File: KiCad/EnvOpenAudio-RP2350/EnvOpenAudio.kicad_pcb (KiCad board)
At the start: 2 copper layers, 21.3 x 68.7 mm, 69 parts, among them J1 USB_C_Receptacle_USB2.0, J2 SM03B-SRSS-TB, J3 Conn_01x10, SW1 B3U-1000, SW2 B3U-1000, U1 W25Q16JVUXIQ, U2 TPS63001DRCR, U3 TLV75518PDBV, U4 RP2350_60QFN, U5 TLV320AIC3100, Y1 ABM8-272-T3

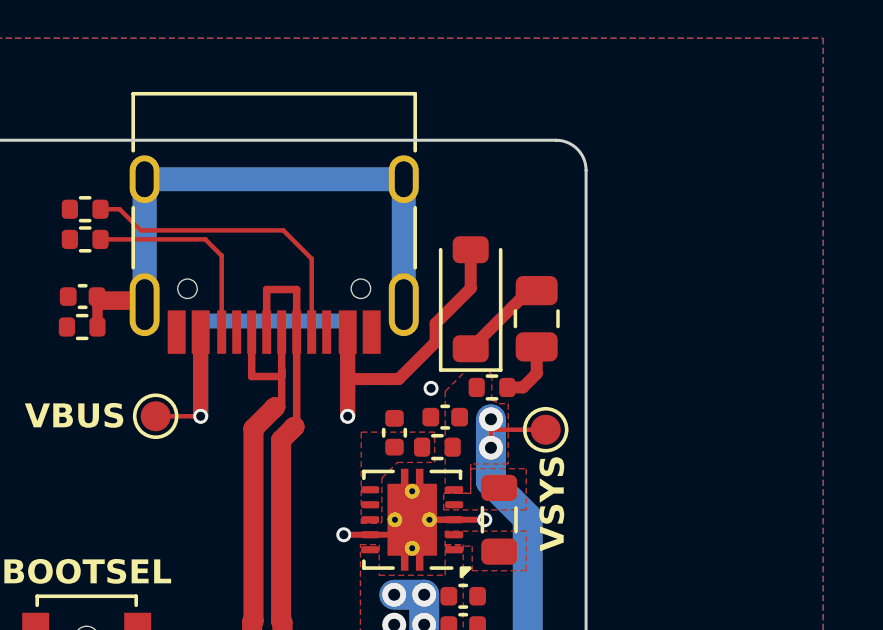
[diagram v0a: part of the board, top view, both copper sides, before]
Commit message: Seperated into RP2040 and RP2350 variants
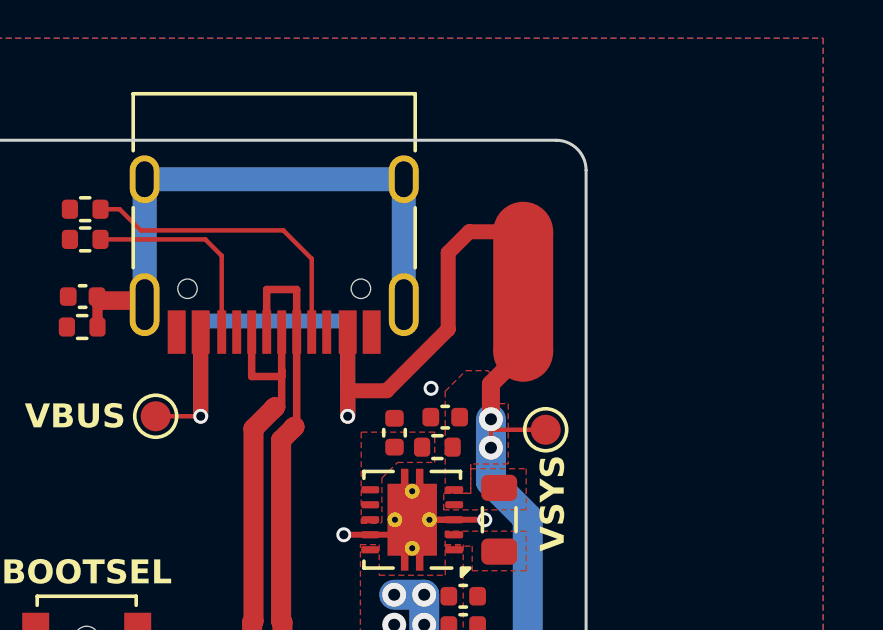
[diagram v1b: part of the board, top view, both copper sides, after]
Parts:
- removed D1: schottky diode low forward voltage, Diode_SMD:D_SOD-123
- removed F1: 0805L050WR, Fuse:Fuse_0805_2012Metric
- removed FB1: FerriteBead 0402, Resistor_SMD:R_0402_1005Metric
- added NT1: NetTie_2, NetTie:NetTie-2_SMD_Pad2.0mm, F.Cu at (74.3, 36.4)
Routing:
- net Net-(D1-K): track 3.00 -> 0.00 mm
- net VSYS: track 67.6 -> 70.3 mm
- net VBUS: track 26.6 -> 28.7 mm
- net Net-(F1-Pad1): track 2.06 -> 0.00 mm
